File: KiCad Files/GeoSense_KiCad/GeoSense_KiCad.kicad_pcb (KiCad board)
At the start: 2 copper layers, 112.5 x 52.5 mm, 0 parts

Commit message: part way through the pcb design
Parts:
- added C1: C_Small, Capacitor_SMD:C_0603_1608Metric_Pad1.08x0.95mm_HandSolder, F.Cu at (29.5, 116.1)
- added C10: C_Small, Capacitor_SMD:C_0603_1608Metric_Pad1.08x0.95mm_HandSolder, F.Cu at (111.6, 66.5)
- added C11: C_Small, Capacitor_SMD:C_0603_1608Metric_Pad1.08x0.95mm_HandSolder, F.Cu at (111.6, 69.0)
- added C12: C_Small, Capacitor_SMD:C_0603_1608Metric_Pad1.08x0.95mm_HandSolder, F.Cu at (111.6, 71.5)
- added C13: C_Small, Capacitor_SMD:C_0603_1608Metric_Pad1.08x0.95mm_HandSolder, F.Cu at (116.0, 59.0)
- added C14: C_Small, Capacitor_SMD:C_0603_1608Metric_Pad1.08x0.95mm_HandSolder, F.Cu at (116.0, 61.5)
- added C15: C_Small, Capacitor_SMD:C_0603_1608Metric_Pad1.08x0.95mm_HandSolder, F.Cu at (116.0, 64.0)
- added C16: C_Small, Capacitor_SMD:C_0603_1608Metric_Pad1.08x0.95mm_HandSolder, F.Cu at (116.0, 66.5)
- added C2: C_Small, Capacitor_SMD:C_0603_1608Metric_Pad1.08x0.95mm_HandSolder, F.Cu at (27.5, 116.1)
- added C3: C_Small, Capacitor_SMD:C_0603_1608Metric_Pad1.08x0.95mm_HandSolder, F.Cu at (107.3, 64.0)
- added C4: C_Small, Capacitor_SMD:C_0603_1608Metric_Pad1.08x0.95mm_HandSolder, F.Cu at (107.3, 66.5)
- added C5: C_Small, Capacitor_SMD:C_0603_1608Metric_Pad1.08x0.95mm_HandSolder, F.Cu at (107.3, 69.0)
- added C6: C_Small, Capacitor_SMD:C_0603_1608Metric_Pad1.08x0.95mm_HandSolder, F.Cu at (107.3, 71.5)
- added C7: C_Small, Capacitor_SMD:C_0603_1608Metric_Pad1.08x0.95mm_HandSolder, F.Cu at (111.6, 59.0)
- added C8: C_Small, Capacitor_SMD:C_0603_1608Metric_Pad1.08x0.95mm_HandSolder, F.Cu at (111.6, 61.5)
- added C9: C_Small, Capacitor_SMD:C_0603_1608Metric_Pad1.08x0.95mm_HandSolder, F.Cu at (111.6, 64.0)
- added J0: Conn_01x04_Pin, Connector_PinHeader_2.54mm:PinHeader_1x04_P2.54mm_Horizontal, F.Cu at (57.2, 16.3)
- added J1: Conn_01x04_Pin, Connector_PinHeader_2.54mm:PinHeader_1x04_P2.54mm_Horizontal, F.Cu at (23.9, 128.3)
- added J10: Conn_01x01_Socket, MountingHole:MountingHole_3.2mm_M3_DIN965_Pad_TopBottom, F.Cu at (76.0, 66.5)
- added J11: Conn_01x01_Socket, MountingHole:MountingHole_3.2mm_M3_DIN965_Pad_TopBottom, F.Cu at (76.0, 73.7)
- added J12: Conn_01x01_Socket, MountingHole:MountingHole_3.2mm_M3_DIN965_Pad_TopBottom, F.Cu at (76.0, 80.8)
- added J13: Conn_01x01_Socket, MountingHole:MountingHole_3.2mm_M3_DIN965_Pad_TopBottom, F.Cu at (76.0, 88.0)
- added J14: Conn_01x04_Pin, Connector_PinHeader_2.54mm:PinHeader_1x04_P2.54mm_Horizontal, F.Cu at (84.0, 40.8)
- added J14: Conn_01x04_Pin, Connector_PinHeader_2.54mm:PinHeader_1x04_P2.54mm_Horizontal, F.Cu at (94.0, 72.3)
- added J15: Conn_01x02_Pin, Connector_PinHeader_2.54mm:PinHeader_1x02_P2.54mm_Vertical, F.Cu at (51.8, 66.7)
- added J2: Conn_01x04_Pin, Connector_PinHeader_2.54mm:PinHeader_1x04_P2.54mm_Horizontal, F.Cu at (25.9, 158.3)
- added J3: Conn_01x04_Pin, Connector_PinHeader_2.54mm:PinHeader_1x04_P2.54mm_Horizontal, F.Cu at (27.5, 183.5)
- added J4: Conn_01x04_Pin, Connector_PinHeader_2.54mm:PinHeader_1x04_P2.54mm_Horizontal, F.Cu at (70.7, 16.3)
- added J5: Conn_01x04_Pin, Connector_PinHeader_2.54mm:PinHeader_1x04_P2.54mm_Horizontal, F.Cu at (70.7, 28.6)
- added J6: Conn_01x04_Pin, Connector_PinHeader_2.54mm:PinHeader_1x04_P2.54mm_Horizontal, F.Cu at (70.7, 40.8)
- added J7: Conn_01x04_Pin, Connector_PinHeader_2.54mm:PinHeader_1x04_P2.54mm_Horizontal, F.Cu at (70.7, 53.0)
- added J8: Conn_01x04_Pin, Connector_PinHeader_2.54mm:PinHeader_1x04_P2.54mm_Horizontal, F.Cu at (84.0, 16.3)
- added J9: Conn_01x04_Pin, Connector_PinHeader_2.54mm:PinHeader_1x04_P2.54mm_Horizontal, F.Cu at (84.0, 28.6)
- added J9: Conn_01x04_Pin, Connector_PinHeader_2.54mm:PinHeader_1x04_P2.54mm_Horizontal, F.Cu at (94.0, 60.0)
- added JP1: SolderJumper_2_Open, Jumper:SolderJumper-2_P1.3mm_Open_RoundedPad1.0x1.5mm, F.Cu at (28.5, 123.8)
- added JP2: SolderJumper_2_Open, Jumper:SolderJumper-2_P1.3mm_Open_RoundedPad1.0x1.5mm, F.Cu at (31.9, 153.0)
- added JP3: SolderJumper_2_Open, Jumper:SolderJumper-2_P1.3mm_Open_RoundedPad1.0x1.5mm, F.Cu at (31.6, 179.7)
- added JP4: SolderJumper_2_Open, Jumper:SolderJumper-2_P1.3mm_Open_RoundedPad1.0x1.5mm, F.Cu at (43.0, 76.8)
- added JP5: SolderJumper_2_Open, Jumper:SolderJumper-2_P1.3mm_Open_RoundedPad1.0x1.5mm, F.Cu at (43.0, 80.3)
- added JP6: SolderJumper_2_Open, Jumper:SolderJumper-2_P1.3mm_Open_RoundedPad1.0x1.5mm, F.Cu at (47.3, 66.2)
- added JP7: SolderJumper_2_Open, Jumper:SolderJumper-2_P1.3mm_Open_RoundedPad1.0x1.5mm, F.Cu at (47.3, 69.7)
- added JP8: SolderJumper_2_Open, Jumper:SolderJumper-2_P1.3mm_Open_RoundedPad1.0x1.5mm, F.Cu at (47.3, 73.2)
- added R1: R, Resistor_THT:R_Axial_DIN0204_L3.6mm_D1.6mm_P5.08mm_Horizontal, F.Cu at (39.0, 121.2)
- added R10: R, Resistor_THT:R_Axial_DIN0204_L3.6mm_D1.6mm_P5.08mm_Horizontal, F.Cu at (46.9, 114.3)
- added R11: R, Resistor_THT:R_Axial_DIN0204_L3.6mm_D1.6mm_P5.08mm_Horizontal, F.Cu at (35.1, 177.2)
- added R12: R, Resistor_THT:R_Axial_DIN0204_L3.6mm_D1.6mm_P5.08mm_Horizontal, F.Cu at (49.6, 170.2)
- added R13: R, Resistor_THT:R_Axial_DIN0204_L3.6mm_D1.6mm_P5.08mm_Horizontal, F.Cu at (38.6, 182.3)
- added R14: R, Resistor_THT:R_Axial_DIN0204_L3.6mm_D1.6mm_P5.08mm_Horizontal, F.Cu at (42.1, 177.2)
- added R15: R, Resistor_THT:R_Axial_DIN0204_L3.6mm_D1.6mm_P5.08mm_Horizontal, F.Cu at (45.6, 172.7)
- added R16: R, Resistor_THT:R_Axial_DIN0204_L3.6mm_D1.6mm_P5.08mm_Horizontal, F.Cu at (45.6, 181.7)
- added R17: R, Resistor_THT:R_Axial_DIN0204_L3.6mm_D1.6mm_P5.08mm_Horizontal, F.Cu at (54.7, 173.7)
- added R18: R, Resistor_THT:R_Axial_DIN0204_L3.6mm_D1.6mm_P5.08mm_Horizontal, F.Cu at (54.2, 185.7)
- added R19: R, Resistor_THT:R_Axial_DIN0204_L3.6mm_D1.6mm_P5.08mm_Horizontal, F.Cu at (61.1, 183.3)
- added R2: R, Resistor_THT:R_Axial_DIN0204_L3.6mm_D1.6mm_P5.08mm_Horizontal, F.Cu at (42.5, 116.8)
- added R20: R, Resistor_THT:R_Axial_DIN0204_L3.6mm_D1.6mm_P5.08mm_Horizontal, F.Cu at (58.1, 178.8)
- added R21: R, Resistor_THT:R_Axial_DIN0204_L3.6mm_D1.6mm_P5.08mm_Horizontal, F.Cu at (24.3, 28.1)
- added R22: R, Resistor_THT:R_Axial_DIN0204_L3.6mm_D1.6mm_P5.08mm_Horizontal, F.Cu at (24.3, 31.3)
- added R23: R, Resistor_THT:R_Axial_DIN0204_L3.6mm_D1.6mm_P5.08mm_Horizontal, F.Cu at (24.3, 34.5)
- added R24: R, Resistor_THT:R_Axial_DIN0204_L3.6mm_D1.6mm_P5.08mm_Horizontal, F.Cu at (24.3, 37.6)
- added R25: R, Resistor_THT:R_Axial_DIN0204_L3.6mm_D1.6mm_P5.08mm_Horizontal, F.Cu at (24.3, 40.8)
- added R26: R, Resistor_THT:R_Axial_DIN0204_L3.6mm_D1.6mm_P5.08mm_Horizontal, F.Cu at (24.3, 43.9)
- added R27: R, Resistor_THT:R_Axial_DIN0204_L3.6mm_D1.6mm_P5.08mm_Horizontal, F.Cu at (24.3, 47.0)
- added R28: R, Resistor_THT:R_Axial_DIN0204_L3.6mm_D1.6mm_P5.08mm_Horizontal, F.Cu at (24.3, 50.2)
- added R29: R, Resistor_THT:R_Axial_DIN0204_L3.6mm_D1.6mm_P5.08mm_Horizontal, F.Cu at (24.3, 53.4)
- added R3: R, Resistor_THT:R_Axial_DIN0204_L3.6mm_D1.6mm_P5.08mm_Horizontal, F.Cu at (42.5, 125.8)
- added R30: R, Resistor_THT:R_Axial_DIN0204_L3.6mm_D1.6mm_P5.08mm_Horizontal, F.Cu at (24.3, 56.5)
- added R31: R, Resistor_THT:R_Axial_DIN0204_L3.6mm_D1.6mm_P5.08mm_Horizontal, F.Cu at (24.3, 59.6)
- added R32: R, Resistor_THT:R_Axial_DIN0204_L3.6mm_D1.6mm_P5.08mm_Horizontal, F.Cu at (24.3, 62.8)
- added R33: R, Resistor_THT:R_Axial_DIN0204_L3.6mm_D1.6mm_P5.08mm_Horizontal, F.Cu at (32.3, 15.6)
- added R34: R, Resistor_THT:R_Axial_DIN0204_L3.6mm_D1.6mm_P5.08mm_Horizontal, F.Cu at (32.3, 18.7)
- added R35: R, Resistor_THT:R_Axial_DIN0204_L3.6mm_D1.6mm_P5.08mm_Horizontal, F.Cu at (32.3, 21.9)
- added R36: R, Resistor_THT:R_Axial_DIN0204_L3.6mm_D1.6mm_P5.08mm_Horizontal, F.Cu at (32.3, 25.0)
- added R37: R, Resistor_THT:R_Axial_DIN0204_L3.6mm_D1.6mm_P5.08mm_Horizontal, F.Cu at (32.3, 28.1)
- added R38: R, Resistor_THT:R_Axial_DIN0204_L3.6mm_D1.6mm_P5.08mm_Horizontal, F.Cu at (32.3, 31.3)
- added R39: R, Resistor_THT:R_Axial_DIN0204_L3.6mm_D1.6mm_P5.08mm_Horizontal, F.Cu at (32.3, 34.5)
- added R4: R, Resistor_THT:R_Axial_DIN0204_L3.6mm_D1.6mm_P5.08mm_Horizontal, F.Cu at (52.1, 129.8)
- added R40: R, Resistor_THT:R_Axial_DIN0204_L3.6mm_D1.6mm_P5.08mm_Horizontal, F.Cu at (32.3, 37.6)
- added R41: R, Resistor_THT:R_Axial_DIN0204_L3.6mm_D1.6mm_P5.08mm_Horizontal, F.Cu at (35.4, 150.6)
- added R42: R, Resistor_THT:R_Axial_DIN0204_L3.6mm_D1.6mm_P5.08mm_Horizontal, F.Cu at (32.3, 43.9)
- added R43: R, Resistor_THT:R_Axial_DIN0204_L3.6mm_D1.6mm_P5.08mm_Horizontal, F.Cu at (32.3, 47.0)
- added R44: R, Resistor_THT:R_Axial_DIN0204_L3.6mm_D1.6mm_P5.08mm_Horizontal, F.Cu at (32.3, 50.2)
- added R45: R, Resistor_THT:R_Axial_DIN0204_L3.6mm_D1.6mm_P5.08mm_Horizontal, F.Cu at (50.6, 143.7)
- added R46: R, Resistor_THT:R_Axial_DIN0204_L3.6mm_D1.6mm_P5.08mm_Horizontal, F.Cu at (32.3, 56.5)
- added R47: R, Resistor_THT:R_Axial_DIN0204_L3.6mm_D1.6mm_P5.08mm_Horizontal, F.Cu at (32.3, 59.6)
- added R48: R, Resistor_THT:R_Axial_DIN0204_L3.6mm_D1.6mm_P5.08mm_Horizontal, F.Cu at (32.3, 62.8)
- added R49: R, Resistor_THT:R_Axial_DIN0204_L3.6mm_D1.6mm_P5.08mm_Horizontal, F.Cu at (38.9, 155.7)
- added R5: R, Resistor_THT:R_Axial_DIN0204_L3.6mm_D1.6mm_P5.08mm_Horizontal, F.Cu at (52.1, 117.8)
- added R50: R, Resistor_THT:R_Axial_DIN0204_L3.6mm_D1.6mm_P5.08mm_Horizontal, F.Cu at (40.3, 18.7)
- added R51: R, Resistor_THT:R_Axial_DIN0204_L3.6mm_D1.6mm_P5.08mm_Horizontal, F.Cu at (40.3, 21.9)
- added R52: R, Resistor_THT:R_Axial_DIN0204_L3.6mm_D1.6mm_P5.08mm_Horizontal, F.Cu at (40.3, 25.0)
- added R53: R, Resistor_THT:R_Axial_DIN0204_L3.6mm_D1.6mm_P5.08mm_Horizontal, F.Cu at (42.9, 150.7)
- added R54: R, Resistor_THT:R_Axial_DIN0204_L3.6mm_D1.6mm_P5.08mm_Horizontal, F.Cu at (40.3, 31.3)
- added R55: R, Resistor_THT:R_Axial_DIN0204_L3.6mm_D1.6mm_P5.08mm_Horizontal, F.Cu at (40.3, 34.5)
- added R56: R, Resistor_THT:R_Axial_DIN0204_L3.6mm_D1.6mm_P5.08mm_Horizontal, F.Cu at (40.3, 37.6)
- added R57: R, Resistor_THT:R_Axial_DIN0204_L3.6mm_D1.6mm_P5.08mm_Horizontal, F.Cu at (46.4, 146.1)
- added R58: R, Resistor_THT:R_Axial_DIN0204_L3.6mm_D1.6mm_P5.08mm_Horizontal, F.Cu at (46.4, 155.2)
- added R59: R, Resistor_THT:R_Axial_DIN0204_L3.6mm_D1.6mm_P5.08mm_Horizontal, F.Cu at (40.3, 47.0)
- added R6: R, Resistor_THT:R_Axial_DIN0204_L3.6mm_D1.6mm_P5.08mm_Horizontal, F.Cu at (55.5, 123.4)
- added R60: R, Resistor_THT:R_Axial_DIN0204_L3.6mm_D1.6mm_P5.08mm_Horizontal, F.Cu at (40.3, 50.2)
- added R61: R, Resistor_THT:R_Axial_DIN0204_L3.6mm_D1.6mm_P5.08mm_Horizontal, F.Cu at (40.3, 53.4)
- added R62: R, Resistor_THT:R_Axial_DIN0204_L3.6mm_D1.6mm_P5.08mm_Horizontal, F.Cu at (40.3, 56.5)
- added R63: R, Resistor_THT:R_Axial_DIN0204_L3.6mm_D1.6mm_P5.08mm_Horizontal, F.Cu at (40.3, 59.6)
- added R64: R, Resistor_THT:R_Axial_DIN0204_L3.6mm_D1.6mm_P5.08mm_Horizontal, F.Cu at (40.3, 62.8)
- added R65: R, Resistor_THT:R_Axial_DIN0204_L3.6mm_D1.6mm_P5.08mm_Horizontal, F.Cu at (55.7, 147.2)
- added R66: R, Resistor_THT:R_Axial_DIN0204_L3.6mm_D1.6mm_P5.08mm_Horizontal, F.Cu at (55.6, 159.2)
- added R67: R, Resistor_THT:R_Axial_DIN0204_L3.6mm_D1.6mm_P5.08mm_Horizontal, F.Cu at (48.4, 21.9)
- added R68: R, Resistor_THT:R_Axial_DIN0204_L3.6mm_D1.6mm_P5.08mm_Horizontal, F.Cu at (48.4, 25.0)
- added R69: R, Resistor_THT:R_Axial_DIN0204_L3.6mm_D1.6mm_P5.08mm_Horizontal, F.Cu at (48.4, 28.1)
- added R7: R, Resistor_THT:R_Axial_DIN0204_L3.6mm_D1.6mm_P5.08mm_Horizontal, F.Cu at (58.0, 126.9)
- added R70: R, Resistor_THT:R_Axial_DIN0204_L3.6mm_D1.6mm_P5.08mm_Horizontal, F.Cu at (48.4, 31.3)
- added R71: R, Resistor_THT:R_Axial_DIN0204_L3.6mm_D1.6mm_P5.08mm_Horizontal, F.Cu at (48.4, 34.5)
- added R72: R, Resistor_THT:R_Axial_DIN0204_L3.6mm_D1.6mm_P5.08mm_Horizontal, F.Cu at (48.4, 37.6)
- added R73: R, Resistor_THT:R_Axial_DIN0204_L3.6mm_D1.6mm_P5.08mm_Horizontal, F.Cu at (62.6, 155.7)
- added R74: R, Resistor_THT:R_Axial_DIN0204_L3.6mm_D1.6mm_P5.08mm_Horizontal, F.Cu at (48.4, 43.9)
- added R75: R, Resistor_THT:R_Axial_DIN0204_L3.6mm_D1.6mm_P5.08mm_Horizontal, F.Cu at (48.4, 47.0)
- added R76: R, Resistor_THT:R_Axial_DIN0204_L3.6mm_D1.6mm_P5.08mm_Horizontal, F.Cu at (48.4, 50.2)
- added R77: R, Resistor_THT:R_Axial_DIN0204_L3.6mm_D1.6mm_P5.08mm_Horizontal, F.Cu at (59.6, 152.2)
- added R78: R, Resistor_THT:R_Axial_DIN0204_L3.6mm_D1.6mm_P5.08mm_Horizontal, F.Cu at (48.4, 56.5)
- added R79: R, Resistor_THT:R_Axial_DIN0204_L3.6mm_D1.6mm_P5.08mm_Horizontal, F.Cu at (48.4, 59.6)
- added R8: R, Resistor_THT:R_Axial_DIN0204_L3.6mm_D1.6mm_P5.08mm_Horizontal, F.Cu at (32.0, 121.3)
- added R80: R, Resistor_THT:R_Axial_DIN0204_L3.6mm_D1.6mm_P5.08mm_Horizontal, F.Cu at (48.4, 62.8)
- added R9: R, Resistor_THT:R_Axial_DIN0204_L3.6mm_D1.6mm_P5.08mm_Horizontal, F.Cu at (35.5, 126.4)
- added U1: LM324, Package_SO:TSSOP-14_4.4x5mm_P0.65mm, F.Cu at (49.5, 123.8)
- added U1.1: LM334Z, Package_TO_SOT_THT:TO-92_Inline, F.Cu at (35.1, 130.8)
- added U1.2: LM334Z, Package_TO_SOT_THT:TO-92_Inline, F.Cu at (32.5, 116.8)
- added U2: LM324, Package_SO:TSSOP-14_4.4x5mm_P0.65mm, F.Cu at (53.1, 153.2)
- added U2.1: LM334Z, Package_TO_SOT_THT:TO-92_Inline, F.Cu at (38.4, 160.3)
- added U2.2: LM334Z, Package_TO_SOT_THT:TO-92_Inline, F.Cu at (35.6, 146.2)
- added U3: LM324, Package_SO:TSSOP-14_4.4x5mm_P0.65mm, F.Cu at (51.6, 179.7)
- added U3.1: LM334Z, Package_TO_SOT_THT:TO-92_Inline, F.Cu at (38.1, 186.7)
- added U3.2: LM334Z, Package_TO_SOT_THT:TO-92_Inline, F.Cu at (35.6, 172.7)
- added U4: LM324, Package_SO:TSSOP-14_4.4x5mm_P0.65mm, F.Cu at (59.3, 86.0)
- added U4.1: LM334Z, Package_TO_SOT_THT:TO-92_Inline, F.Cu at (23.3, 79.2)
- added U4.2: LM334Z, Package_TO_SOT_THT:TO-92_Inline, F.Cu at (23.3, 85.0)
- added U5: LM324, Package_SO:TSSOP-14_4.4x5mm_P0.65mm, F.Cu at (59.3, 92.6)
- added U5.1: LM334Z, Package_TO_SOT_THT:TO-92_Inline, F.Cu at (29.8, 67.6)
- added U5.2: LM334Z, Package_TO_SOT_THT:TO-92_Inline, F.Cu at (29.8, 73.4)
- added U6: LM324, Package_SO:TSSOP-14_4.4x5mm_P0.65mm, F.Cu at (68.0, 66.3)
- added U6.1: LM334Z, Package_TO_SOT_THT:TO-92_Inline, F.Cu at (29.8, 79.2)
- added U6.2: LM334Z, Package_TO_SOT_THT:TO-92_Inline, F.Cu at (29.8, 85.0)
- added U7: LM324, Package_SO:TSSOP-14_4.4x5mm_P0.65mm, F.Cu at (68.0, 72.8)
- added U7.1: LM334Z, Package_TO_SOT_THT:TO-92_Inline, F.Cu at (36.3, 67.6)
- added U7.2: LM334Z, Package_TO_SOT_THT:TO-92_Inline, F.Cu at (36.3, 73.4)
- added U8: LM324, Package_SO:TSSOP-14_4.4x5mm_P0.65mm, F.Cu at (68.0, 79.4)
- added U8.1: LM334Z, Package_TO_SOT_THT:TO-92_Inline, F.Cu at (36.3, 79.2)
- added U8.2: LM334Z, Package_TO_SOT_THT:TO-92_Inline, F.Cu at (36.3, 85.0)
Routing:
- net T2.C: track 0.00 -> 27.2 mm
- net T1.C: track 0.00 -> 26.9 mm
- net T3.C: track 0.00 -> 26.5 mm
- net T2.2 In: track 0.00 -> 19.0 mm
- net T1.2 In: track 0.00 -> 18.7 mm
- net T3.2 In: track 0.00 -> 17.7 mm
- net Net-(U2C-+): track 0.00 -> 14.9 mm
- net Net-(U3C-+): track 0.00 -> 14.7 mm
- net Net-(U1C-+): track 0.00 -> 13.7 mm
- net Net-(U2C--): track 0.00 -> 13.2 mm
- net Net-(R41-Pad1): track 0.00 -> 12.9 mm, vias 0 -> 1
- net Net-(R49-Pad1): track 0.00 -> 12.8 mm, vias 0 -> 1
- net Net-(U3C--): track 0.00 -> 12.8 mm
- net Net-(R13-Pad1): track 0.00 -> 12.4 mm, vias 0 -> 1
- net Net-(R11-Pad1): track 0.00 -> 12.3 mm, vias 0 -> 1
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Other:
- board text added: "Module 1"
- board text added: "Module 2"
- board text added: "Module 3"

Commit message: pcb mainly built
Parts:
- removed C10, C11, C12, C13, C14, C15, C16, C9: C_Small, Capacitor_SMD:C_0603_1608Metric_Pad1.08x0.95mm_HandSolder
- removed the J14 at (84.0, 40.8)
- removed the J9 at (84.0, 28.6)
- C1, C2, C3, C4, C5, C6, C7, C8: footprint Capacitor_SMD:C_0603_1608Metric_Pad1.08x0.95mm_HandSolder -> Capacitor_SMD:C_0603_1608Metric; moved to B.Cu
- J0, J1, J14, J2, J3, J4, J5, J6, J7, J8, J9: footprint Connector_PinHeader_2.54mm:PinHeader_1x04_P2.54mm_Horizontal -> Connector_PinHeader_2.54mm:PinHeader_1x04_P2.54mm_Vertical
- moved J0 183.9 mm to (202.5, 129.0), turned to 180 degrees
- moved R52 170.5 mm to (180.3, 122.4), turned to 180 degrees
- moved JP1 163.7 mm to (175.2, 51.2), turned to 180 degrees
- moved U1.2 161.9 mm to (182.2, 55.2), turned to -90 degrees
- moved R44 161.7 mm to (175.3, 125.9)
- moved R8 160.2 mm to (177.7, 54.8), turned to 180 degrees
- moved J15 158.5 mm to (202.5, 116.0), turned to 180 degrees
- moved R56 157.5 mm to (175.3, 118.9)
- moved R36 157.1 mm to (155.5, 122.5), turned to 180 degrees
- moved R38 156.5 mm to (161.5, 119.6), turned to 90 degrees
- moved U8.1 154.8 mm to (184.8, 122.6), turned to -90 degrees
- moved R9 153.1 mm to (172.6, 58.3), turned to 0 degrees
- moved R35 152.5 mm to (156.0, 111.0), turned to 180 degrees
- moved U1.1 151.8 mm to (168.2, 57.8), turned to 90 degrees
- moved R72 151.7 mm to (183.3, 106.9), turned to -90 degrees
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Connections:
- C1 pad 2: T1.C -> +5V
- C2 pad 1: T1.2 In -> GND
- C2 pad 2: GND -> +5V
- C3 pad 2: T2.C -> +5V
- C4 pad 1: T2.2 In -> GND
- C4 pad 2: GND -> +5V
- C5 pad 2: T3.C -> +5V
- C6 pad 1: T3.2 In -> GND
- C6 pad 2: GND -> +5V
- C7 pad 2: T4.C -> +5V
- C8 pad 1: T4.2 In -> GND
- C8 pad 2: GND -> +5V
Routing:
- net Out 4: track 0.00 -> 103.9 mm
- net T8.2 In: track 0.00 -> 99.8 mm, vias 0 -> 1
- net T8.1 In: track 0.00 -> 96.1 mm
- net Out 3: track 4.84 -> 97.5 mm
- net Out 2: track 4.83 -> 88.6 mm
- net T1.1 In: track 8.97 -> 91.2 mm
- net T1.2 In: track 18.7 -> 99.8 mm
- net T5.2 In: track 0.00 -> 78.8 mm, vias 0 -> 1
- net T6.2 In: track 0.00 -> 71.4 mm, vias 0 -> 1
- net Out 7: track 0.00 -> 70.6 mm
- net T5.1 In: track 0.00 -> 70.4 mm, vias 0 -> 1
- net T7.2 In: track 0.00 -> 67.3 mm, vias 0 -> 1
- net T6.1 In: track 0.00 -> 62.2 mm, vias 0 -> 1
- net T7.1 In: track 0.00 -> 58.9 mm, vias 0 -> 1
- net Out 5: track 0.00 -> 56.9 mm
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- added copper zone on F.Cu, net +5V
- added copper zone on B.Cu, net GND
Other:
- board size 112.5 x 52.5 mm -> 120.5 x 97 mm
- board text removed: "Module 1"
- board text removed: "Module 2"
- board text removed: "Module 3"

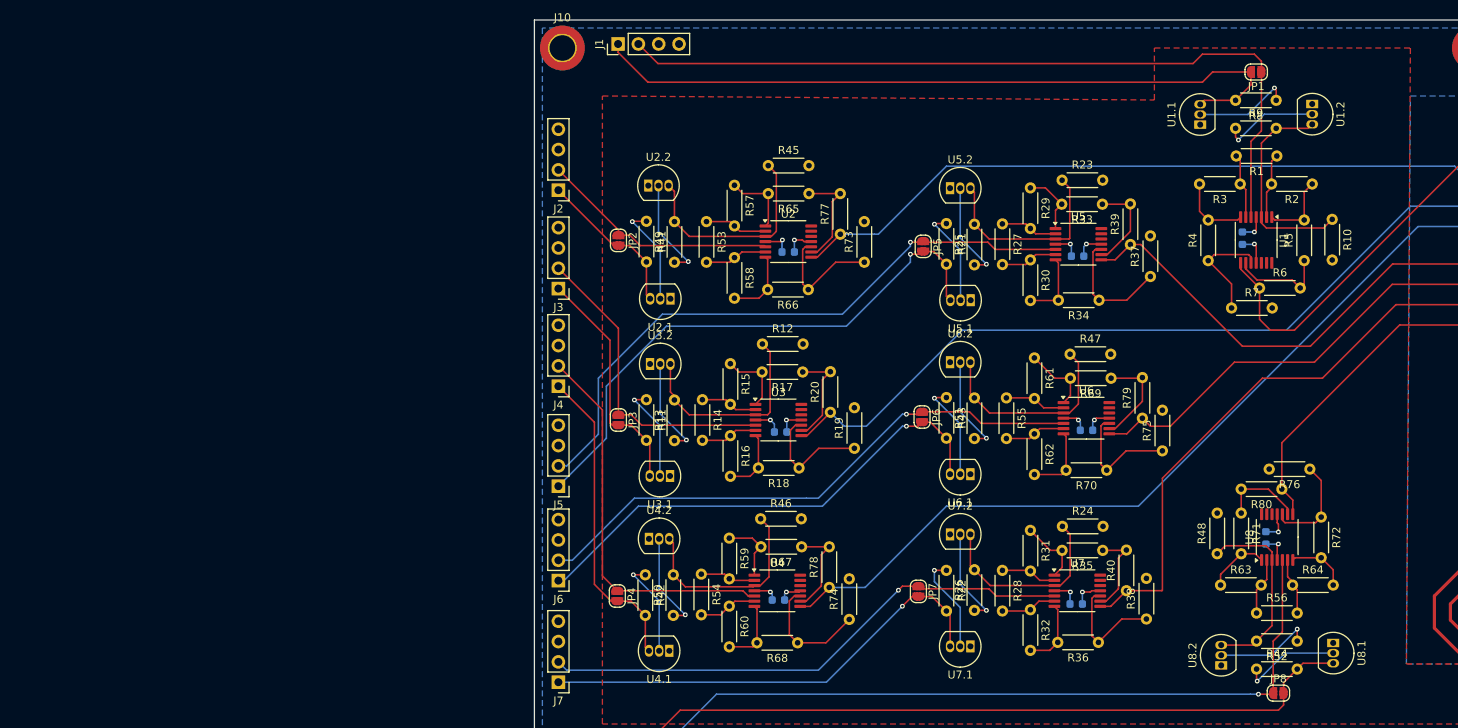
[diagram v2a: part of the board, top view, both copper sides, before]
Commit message: added to diodes to the schematic
need to reroute the pcb
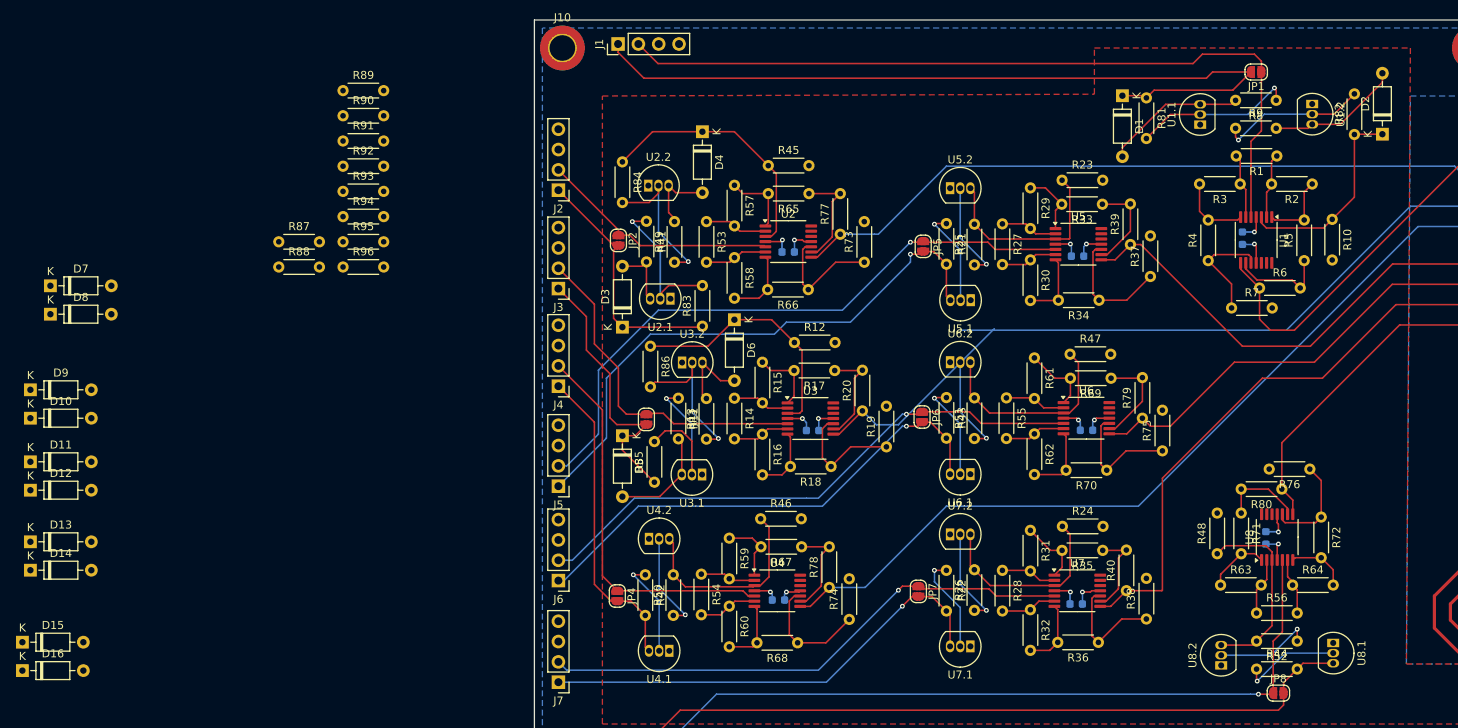
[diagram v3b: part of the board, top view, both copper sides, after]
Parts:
- added D1: D, Diode_THT:D_DO-35_SOD27_P7.62mm_Horizontal, F.Cu at (158.5, 54.2)
- added D10: D, Diode_THT:D_DO-35_SOD27_P7.62mm_Horizontal, F.Cu at (22.0, 94.5)
- added D11: D, Diode_THT:D_DO-35_SOD27_P7.62mm_Horizontal, F.Cu at (22.0, 100.0)
- added D12: D, Diode_THT:D_DO-35_SOD27_P7.62mm_Horizontal, F.Cu at (22.0, 103.5)
- added D13: D, Diode_THT:D_DO-35_SOD27_P7.62mm_Horizontal, F.Cu at (22.0, 110.0)
- added D14: D, Diode_THT:D_DO-35_SOD27_P7.62mm_Horizontal, F.Cu at (22.0, 113.5)
- added D15: D, Diode_THT:D_DO-35_SOD27_P7.62mm_Horizontal, F.Cu at (21.0, 122.5)
- added D16: D, Diode_THT:D_DO-35_SOD27_P7.62mm_Horizontal, F.Cu at (21.0, 126.0)
- added D2: D, Diode_THT:D_DO-35_SOD27_P7.62mm_Horizontal, F.Cu at (191.0, 59.0)
- added D3: D, Diode_THT:D_DO-35_SOD27_P7.62mm_Horizontal, F.Cu at (96.0, 83.1)
- added D4: D, Diode_THT:D_DO-35_SOD27_P7.62mm_Horizontal, F.Cu at (106.0, 58.7)
- added D5: D, Diode_THT:D_DO-35_SOD27_P7.62mm_Horizontal, F.Cu at (96.0, 96.7)
- added D6: D, Diode_THT:D_DO-35_SOD27_P7.62mm_Horizontal, F.Cu at (110.0, 82.2)
- added D7: D, Diode_THT:D_DO-35_SOD27_P7.62mm_Horizontal, F.Cu at (24.5, 78.0)
- added D8: D, Diode_THT:D_DO-35_SOD27_P7.62mm_Horizontal, F.Cu at (24.5, 81.5)
- added D9: D, Diode_THT:D_DO-35_SOD27_P7.62mm_Horizontal, F.Cu at (22.0, 91.0)
- added R81: R, Resistor_THT:R_Axial_DIN0204_L3.6mm_D1.6mm_P5.08mm_Horizontal, F.Cu at (161.5, 54.5)
- added R82: R, Resistor_THT:R_Axial_DIN0204_L3.6mm_D1.6mm_P5.08mm_Horizontal, F.Cu at (187.5, 59.0)
- added R83: R, Resistor_THT:R_Axial_DIN0204_L3.6mm_D1.6mm_P5.08mm_Horizontal, F.Cu at (106.0, 83.0)
- added R84: R, Resistor_THT:R_Axial_DIN0204_L3.6mm_D1.6mm_P5.08mm_Horizontal, F.Cu at (96.0, 62.5)
- added R85: R, Resistor_THT:R_Axial_DIN0204_L3.6mm_D1.6mm_P5.08mm_Horizontal, F.Cu at (100.0, 102.5)
- added R86: R, Resistor_THT:R_Axial_DIN0204_L3.6mm_D1.6mm_P5.08mm_Horizontal, F.Cu at (99.5, 85.5)
- added R87: R, Resistor_THT:R_Axial_DIN0204_L3.6mm_D1.6mm_P5.08mm_Horizontal, F.Cu at (53.0, 72.5)
- added R88: R, Resistor_THT:R_Axial_DIN0204_L3.6mm_D1.6mm_P5.08mm_Horizontal, F.Cu at (53.0, 75.6)
- added R89: R, Resistor_THT:R_Axial_DIN0204_L3.6mm_D1.6mm_P5.08mm_Horizontal, F.Cu at (61.1, 53.5)
- added R90: R, Resistor_THT:R_Axial_DIN0204_L3.6mm_D1.6mm_P5.08mm_Horizontal, F.Cu at (61.1, 56.7)
- added R91: R, Resistor_THT:R_Axial_DIN0204_L3.6mm_D1.6mm_P5.08mm_Horizontal, F.Cu at (61.1, 59.9)
- added R92: R, Resistor_THT:R_Axial_DIN0204_L3.6mm_D1.6mm_P5.08mm_Horizontal, F.Cu at (61.1, 63.0)
- added R93: R, Resistor_THT:R_Axial_DIN0204_L3.6mm_D1.6mm_P5.08mm_Horizontal, F.Cu at (61.1, 66.2)
- added R94: R, Resistor_THT:R_Axial_DIN0204_L3.6mm_D1.6mm_P5.08mm_Horizontal, F.Cu at (61.1, 69.3)
- added R95: R, Resistor_THT:R_Axial_DIN0204_L3.6mm_D1.6mm_P5.08mm_Horizontal, F.Cu at (61.1, 72.5)
- added R96: R, Resistor_THT:R_Axial_DIN0204_L3.6mm_D1.6mm_P5.08mm_Horizontal, F.Cu at (61.1, 75.6)
- moved R11 4.00 mm to (103.0, 92.0)
- moved R14 4.00 mm to (110.0, 92.0)
- moved R15 4.00 mm to (113.5, 87.5)
- moved R16 4.00 mm to (113.5, 96.5)
- moved R19 4.00 mm to (129.0, 98.1)
- moved R20 4.00 mm to (126.0, 93.6)
- moved C3 4.00 mm to (119.8, 96.0)
- moved R12 4.00 mm to (117.5, 85.0)
- moved R13 4.00 mm to (106.5, 97.1)
- moved R17 4.00 mm to (122.5, 88.5)
- moved R18 4.00 mm to (122.1, 100.5)
- moved U3 4.00 mm to (119.5, 94.5)
- moved U3.1 4.00 mm to (106.0, 101.5)
- moved U3.2 4.00 mm to (103.5, 87.5)
- moved JP3 3.50 mm to (99.0, 94.7)
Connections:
- R11 pad 2: T3.1 In -> Net-(D5-A)
- R13 pad 2: T3.C -> Net-(D6-A)
- R21 pad 2: T5.1 In -> Net-(D9-A)
- R22 pad 2: T7.1 In -> Net-(D13-A)
- R25 pad 2: T5.C -> Net-(D10-A)
- R26 pad 2: T7.C -> Net-(D14-A)
- R41 pad 2: T2.1 In -> Net-(D3-A)
- R42 pad 2: T4.1 In -> Net-(D7-A)
- R43 pad 2: T6.1 In -> Net-(D11-A)
- R44 pad 2: T8.1 In -> Net-(D15-A)
- R49 pad 2: T2.C -> Net-(D4-A)
- R50 pad 2: T4.C -> Net-(D8-A)
- R51 pad 2: T6.C -> Net-(D12-A)
- R52 pad 2: T8.C -> Net-(D16-A)
- R8 pad 2: T1.1 In -> Net-(D1-A)
- R9 pad 2: T1.C -> Net-(D2-A)
- U1.1 pad 3: T1.1 In -> Net-(D1-A)
- U1.2 pad 3: T1.C -> Net-(D2-A)
- U2.1 pad 3: T2.1 In -> Net-(D3-A)
- U2.2 pad 3: T2.C -> Net-(D4-A)
- U3.1 pad 3: T3.1 In -> Net-(D5-A)
- U3.2 pad 3: T3.C -> Net-(D6-A)
- U4.1 pad 3: T4.1 In -> Net-(D7-A)
- U4.2 pad 3: T4.C -> Net-(D8-A)
- U5.1 pad 3: T5.1 In -> Net-(D9-A)
- U5.2 pad 3: T5.C -> Net-(D10-A)
- U6.1 pad 3: T6.1 In -> Net-(D11-A)
- U6.2 pad 3: T6.C -> Net-(D12-A)
- U7.1 pad 3: T7.1 In -> Net-(D13-A)
- U7.2 pad 3: T7.C -> Net-(D14-A)
- U8.1 pad 3: T8.1 In -> Net-(D15-A)
- U8.2 pad 3: T8.C -> Net-(D16-A)
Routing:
- net Net-(D1-A): track 0.00 -> 17.3 mm
- net Net-(D2-A): track 0.00 -> 16.8 mm
- net Net-(D5-A): track 0.00 -> 13.2 mm
- net T2.1 In: track 19.5 -> 31.5 mm
- net Net-(D6-A): track 0.00 -> 10.4 mm
- net Net-(R11-Pad1): track 12.3 -> 22.3 mm
- net Net-(D4-A): track 0.00 -> 9.22 mm
- net T1.1 In: track 91.2 -> 99.3 mm
- net Net-(R8-Pad1): track 12.3 -> 20.3 mm
- net Net-(R13-Pad1): track 12.4 -> 19.9 mm
- net Net-(D3-A): track 0.00 -> 7.45 mm
- net Net-(R82-Pad2): track 12.2 -> 18.5 mm
- net Net-(R41-Pad1): track 12.9 -> 19.2 mm
- net Net-(R49-Pad1): track 12.8 -> 18.7 mm
- net T3.1 In: track 29.5 -> 34.8 mm
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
